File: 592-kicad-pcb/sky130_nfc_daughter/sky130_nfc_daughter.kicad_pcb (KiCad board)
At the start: 4 copper layers, 50 x 52 mm, 104 parts, among them J1 U.FL-R-SMT-1_80_, J10 U.FL-R-SMT-1_80_, J2 U.FL-R-SMT-1_80_, J3 U.FL-R-SMT-1_80_, J4 U.FL-R-SMT-1_80_, J5 U.FL-R-SMT-1_80_, J6 U.FL-R-SMT-1_80_, J7 U.FL-R-SMT-1_80_, J8 DF40C-40DS-0.4V_51_, J9 DF40C-40DS-0.4V_51_, SW1 SW_Push, U1 Caravel_QFN, U3 W25Q32JVZP

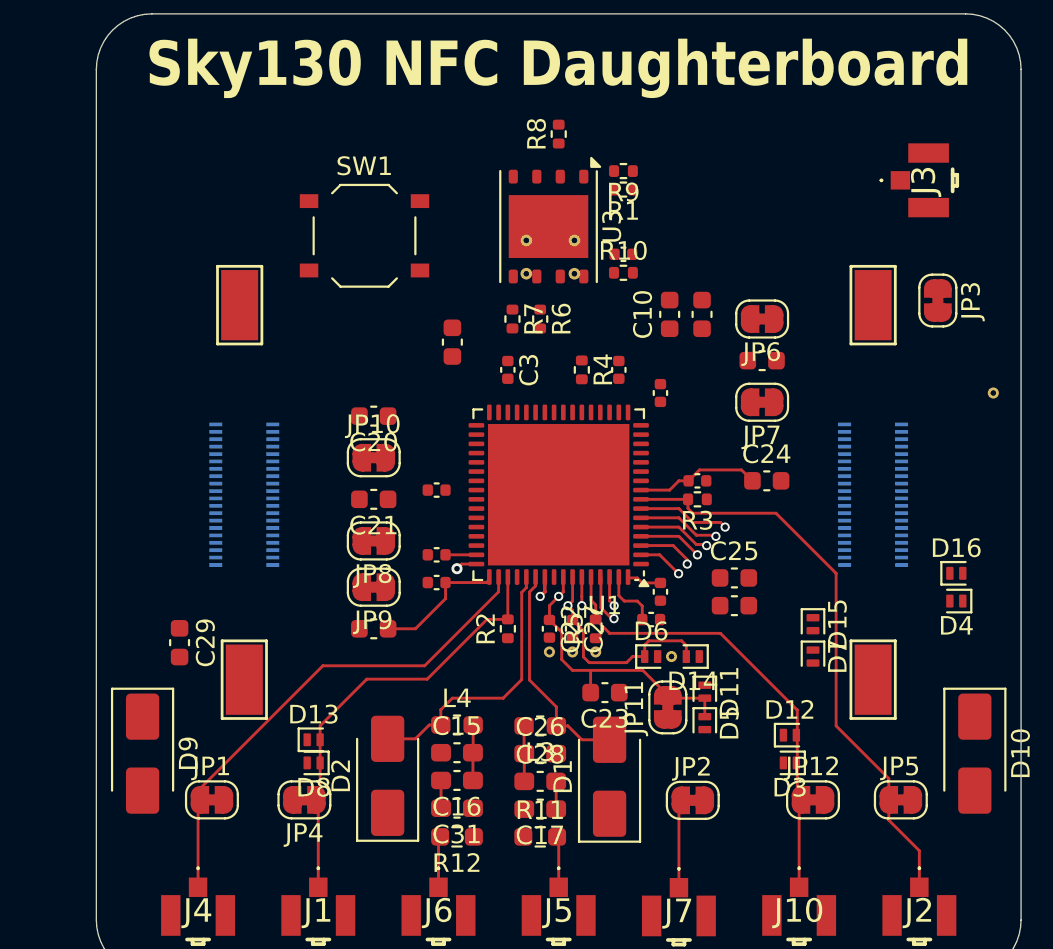
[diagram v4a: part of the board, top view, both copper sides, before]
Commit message: daughterboard routing, changed some mezzanine pins - more to come
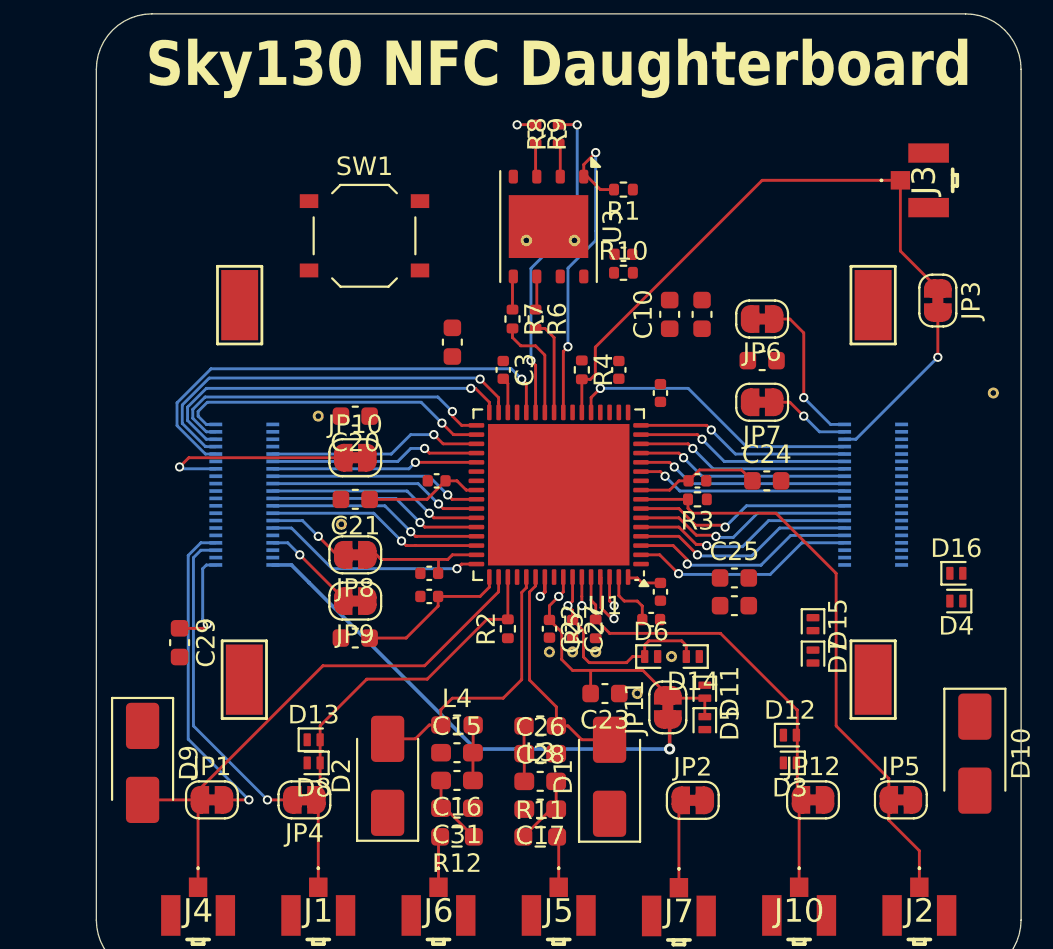
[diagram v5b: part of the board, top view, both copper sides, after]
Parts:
- removed the STITCHM1 at (75.3, 34.0)
- removed the STITCHM1 at (72.8, 34.0)
- added REF**: STITCHING_VIA_0p3mm, 592-partslib:STITCHING_VIA_0p3mm, F.Cu at (62.8, 47.6)
- added REF**: STITCHING_VIA_0p3mm, 592-partslib:STITCHING_VIA_0p3mm, F.Cu at (78.8, 56.8)
- added REF**: STITCHING_VIA_0p3mm, 592-partslib:STITCHING_VIA_0p3mm, F.Cu at (61.5, 41.8)
- moved R9 5.15 mm to (73.2, 26.5), turned to -90 degrees
- moved JP8 1.25 mm to (63.5, 49.2)
- moved JP9 1.25 mm to (63.5, 51.8)
- moved C18 1.12 mm to (63.5, 53.8)
- moved C11 1.08 mm to (67.5, 50.2)
- moved C20 1.00 mm to (63.5, 41.8)
- moved C21 1.00 mm to (63.5, 46.2)
- moved JP10 1.00 mm to (63.5, 44.0)
- moved C6 0.85 mm to (67.5, 51.5)
- moved C12 0.50 mm to (67.9, 45.2)
- moved D9 0.50 mm to (52.0, 60.5)
- moved C3 0.25 mm to (71.5, 39.2)
- moved R6 0.25 mm to (73.2, 36.5)
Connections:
- J8 pad 10: /jtag_TDO -> /gpio
- J8 pad 15: GND -> /spi_0_sck
- J8 pad 16: /spi_0_sck -> GND
- J8 pad 17: GND -> /reset_io
- J8 pad 18: /reset_io -> GND
- J8 pad 2: /gpio -> /jtag_TDO
- J8 pad 23: GND -> /i2c_0_sda
- J8 pad 24: /i2c_0_sda -> GND
- J8 pad 25: GND -> /i2c_0_scl
- J8 pad 26: /i2c_0_scl -> GND
- J8 pad 29: GND -> /tdo2
- J8 pad 3: /c_sel_inc -> GND
- J8 pad 30: /tdo2 -> GND
- J8 pad 4: /jtag_TCK -> /jtag_TDI
- J8 pad 8: /jtag_TDI -> /jtag_TCK
- J9 pad 10: GND -> /spi_flash_0_dq_3
- J9 pad 11: /spi_flash_0_dq_2 -> GND
- J9 pad 12: GND -> /spi_flash_0_dq_2
- J9 pad 13: /spi_flash_0_dq_1 -> GND
- J9 pad 14: GND -> /spi_flash_0_dq_1
- J9 pad 15: /spi_flash_0_dq_0 -> GND
- J9 pad 16: GND -> /spi_flash_0_dq_0
- J9 pad 17: /spi_flash_0_cs_0 -> GND
- J9 pad 18: GND -> /spi_flash_0_cs_0
- J9 pad 19: /spi_flash_0_sck -> GND
- J9 pad 20: /J_ext_clk_dig -> /spi_flash_0_sck
- J9 pad 22: /ext_reset_dig -> /J_ext_clk_dig
- J9 pad 24: GND -> /ext_reset_dig
- J9 pad 27: /TMS_EXT -> GND
- J9 pad 29: /TCK_EXT -> /RESET_EXT
- J9 pad 30: GND -> /TMS_EXT
- J9 pad 31: /TRST_EXT -> /J_FS_EXT
- J9 pad 32: /J_FS_EXT -> /TCK_EXT
- J9 pad 34: /RESET_EXT -> /TRST_EXT
- J9 pad 5: /J_clk -> GND
- J9 pad 6: GND -> /J_clk
- J9 pad 7: /reset_b -> GND
- J9 pad 8: GND -> /reset_b
- J9 pad 9: /spi_flash_0_dq_3 -> GND
- STITCHM1 pad 1: (no net) -> GND (x2)
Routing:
- net /clk: track 0.00 -> 31.0 mm
- net Net-(JP11-A): track 0.00 -> 27.2 mm, vias 0 -> 1
- net /gpio: track 0.00 -> 25.5 mm, vias 0 -> 1
- net /jtag_TCK: track 0.00 -> 22.3 mm, vias 0 -> 1
- net /jtag_TMS: track 0.00 -> 20.3 mm, vias 0 -> 1
- net /jtag_TDI: track 0.00 -> 18.4 mm, vias 0 -> 1
- net /flash_csb: track 0.00 -> 18.3 mm, vias 0 -> 2
- net /J_ANA_MUX_OUT_EXT: track 0.00 -> 17.7 mm, vias 0 -> 1
- net /flash_io1: track 0.00 -> 17.7 mm, vias 0 -> 2
- net /J_clock_uncore: track 0.00 -> 17.5 mm, vias 0 -> 1
- net /jtag_TDO: track 0.00 -> 17.4 mm, vias 0 -> 1
- net /reset_b: track 0.00 -> 16.0 mm, vias 0 -> 1
- net vdda_user_3v3: track 8.39 -> 20.2 mm
- net /i2c_0_scl: track 0.00 -> 11.7 mm, vias 0 -> 1
- net /i2c_0_sda: track 0.00 -> 11.7 mm, vias 0 -> 1
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
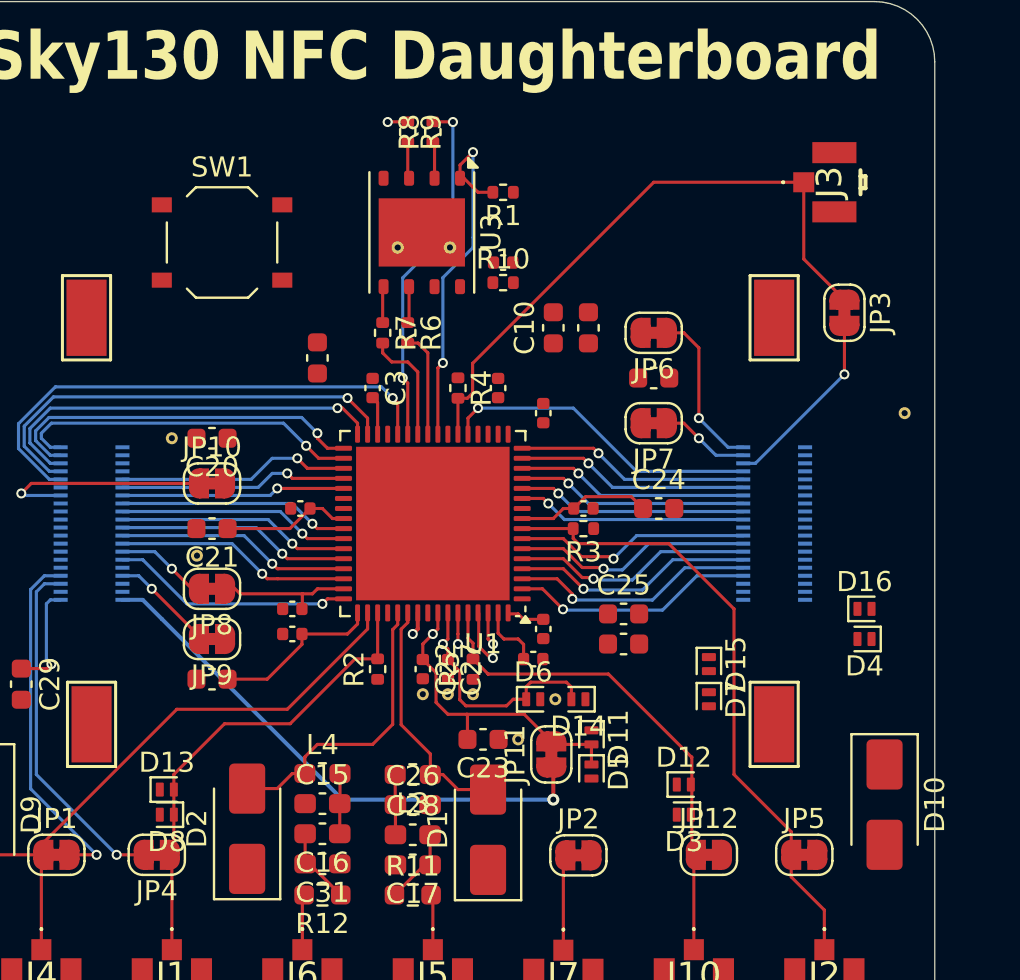
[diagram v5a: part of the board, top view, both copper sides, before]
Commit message: complete signal routing on daughterboard, TODO: power/gnd connections
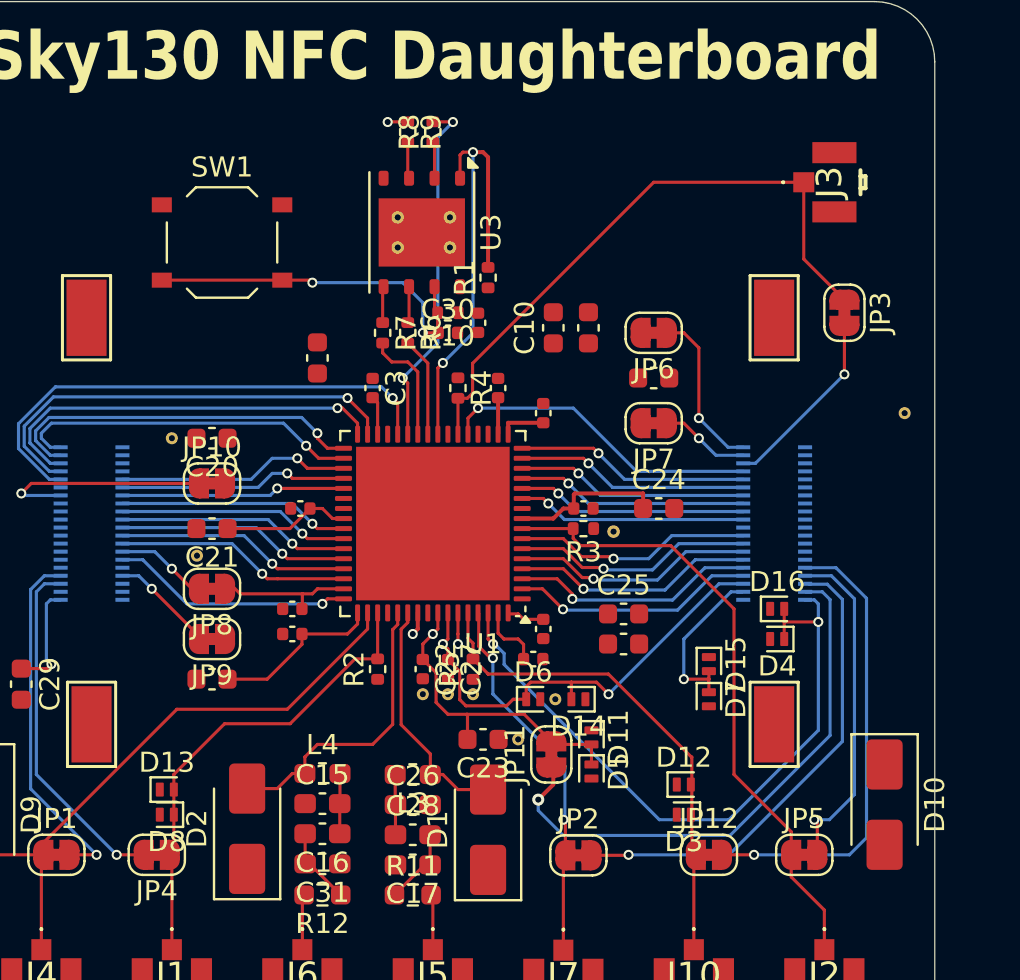
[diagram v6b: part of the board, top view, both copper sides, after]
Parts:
- added C30: 0.1uf, Capacitor_SMD:C_0402_1005Metric, F.Cu at (75.2, 36.5)
- added STITCHM1: StitchingVia-0.3mm, flyingcarsfootprints:StitchingVia-0.3mm, F.Cu at (72.8, 30.8)
- added STITCHM1: StitchingVia-0.3mm, flyingcarsfootprints:StitchingVia-0.3mm, F.Cu at (83.5, 46.4)
- added STITCHM1: StitchingVia-0.3mm, flyingcarsfootprints:StitchingVia-0.3mm, F.Cu at (75.3, 30.8)
- moved D16 4.35 mm to (91.7, 50.2)
- moved D4 4.35 mm to (91.7, 51.8)
- moved R1 4.32 mm to (77.2, 33.8), turned to 90 degrees
- moved C9 3.25 mm to (76.8, 36.0), turned to 90 degrees
- moved R10 3.13 mm to (75.2, 35.5), turned to 180 degrees
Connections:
- net Net-(JP10-A) renamed /JA_vdda_user_3v3
- net Net-(JP6-A) renamed /J_vccd_mgmt_1v8
- net Net-(JP7-A) renamed /J_vddio_vdda_mgmt_3v3
- net Net-(JP8-B) renamed /JB_vdda_user_3v3
- net Net-(JP9-B) renamed /J_vccd_user_1v8
- J8 pad 39: Net-(JP11-A) -> GND
- J9 pad 22: /J_ext_clk_dig -> GND
- J9 pad 29: /RESET_EXT -> GND
- J9 pad 33: /NFC_AFE_TDO_EXT -> /J_ext_clk_dig
- J9 pad 36: GND -> /VREF_EXT
- J9 pad 37: GND -> /J_VDD_EXT
- J9 pad 38: /VREF_EXT -> /RESET_EXT
- J9 pad 39: GND -> /NFC_AFE_TDO_EXT
- JP11 pad 1: Net-(JP11-A) -> /J_VDD_EXT
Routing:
- net /NFC_AFE_TDO_EXT: track 1.65 -> 33.9 mm, vias 1 -> 2
- net /J_VDD_EXT: track 0.00 -> 27.8 mm, vias 0 -> 1
- net Net-(JP11-A): track 27.2 -> 0.00 mm, vias 1 -> 0
- net /J_ANA_MUX_OUT_2_EXT: track 0.00 -> 24.1 mm, vias 0 -> 1
- net /J_FS_EXT: track 0.00 -> 23.2 mm, vias 0 -> 1
- net /flash_rstb: track 0.00 -> 18.1 mm, vias 0 -> 2
- net /J_ext_clk_dig: track 0.00 -> 17.0 mm, vias 0 -> 1
- net /VREF_EXT: track 12.0 -> 23.5 mm, vias 1 -> 2
- net /ANA_MUX_OUT_2_EXT: track 7.39 -> 18.8 mm, vias 1 -> 2
- net /RESET_EXT: track 1.55 -> 9.78 mm, vias 1 -> 2
- net /flash_csb: track 18.3 -> 23.0 mm
- net vddio_vdda_mgmt_3v3: track 4.81 -> 7.13 mm
- net vccd_mgmt_1v8: track 0.00 -> 1.82 mm
- net vdda_user_3v3: track 20.2 -> 21.2 mm

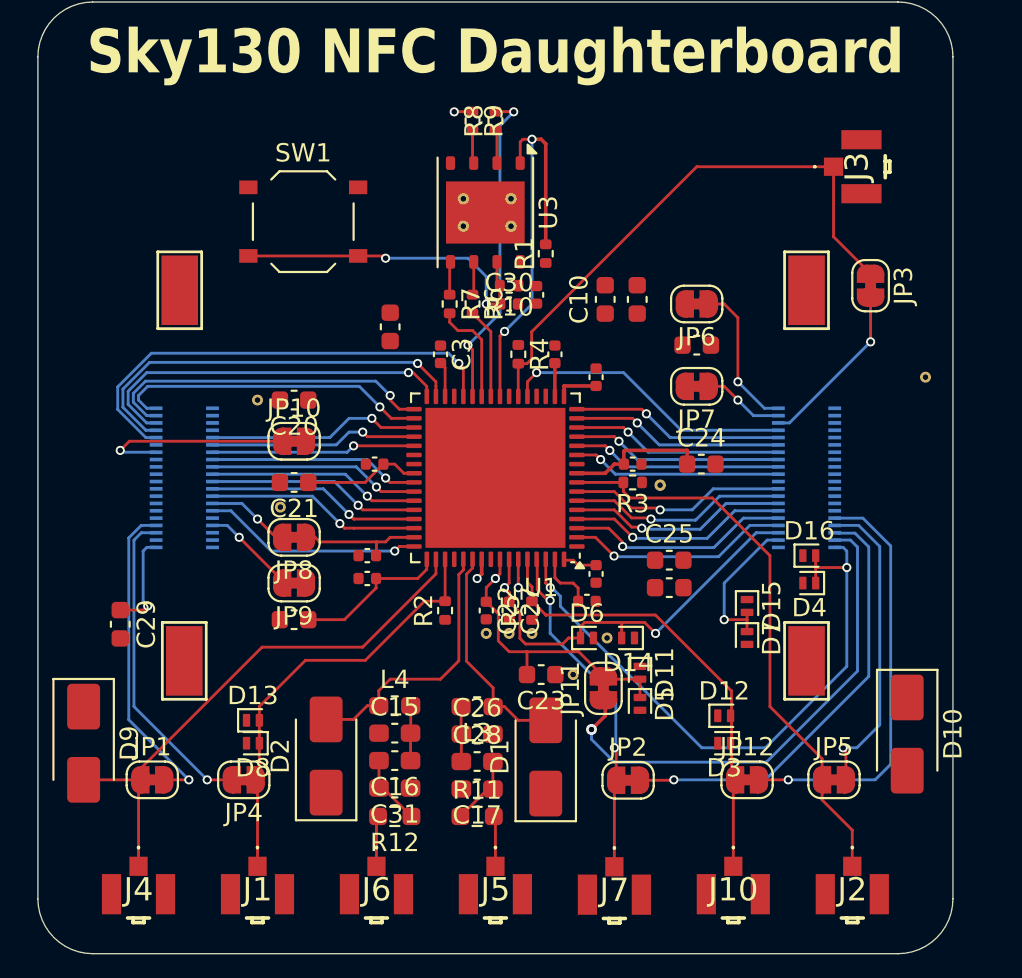
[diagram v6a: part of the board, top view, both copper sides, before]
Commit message: more daughterboard routing, power focus
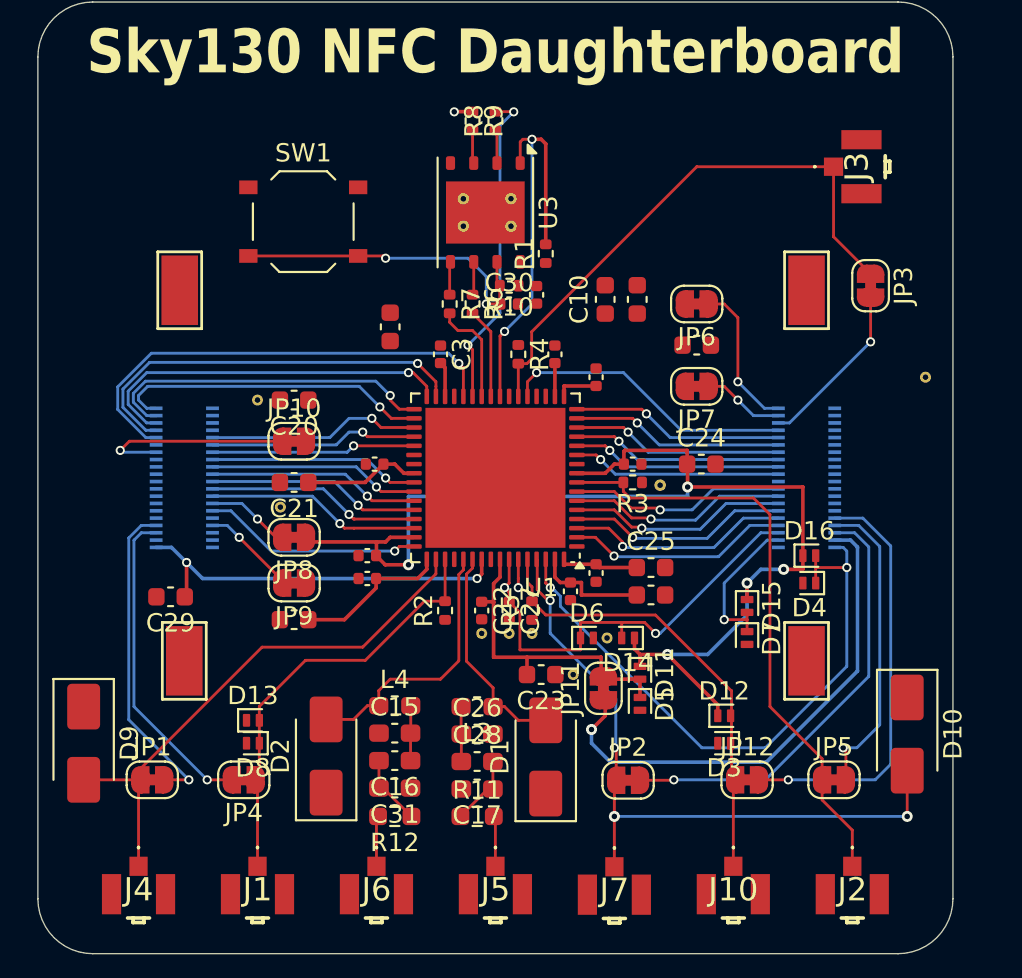
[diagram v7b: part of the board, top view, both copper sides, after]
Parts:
- moved C29 3.13 mm to (56.8, 52.5), turned to 180 degrees
- moved C14 1.08 mm to (83.0, 52.4)
- moved C25 1.08 mm to (83.0, 50.9)
- moved C5 1.05 mm to (78.6, 52.2), turned to 90 degrees
- moved C22 0.25 mm to (73.8, 53.2)
- moved REF** 0.25 mm to (73.8, 54.5)
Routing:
- net vdda_user_3v3: track 21.2 -> 74.0 mm, vias 0 -> 5
- net /ANA_MUX_OUT_2_EXT: track 18.8 -> 37.3 mm, vias 2 -> 4
- net /VRECT_OUT_EXT: track 6.64 -> 21.3 mm
- net vccd_user_1v8: track 11.7 -> 14.7 mm
- net vddio_vdda_mgmt_3v3: track 7.13 -> 9.89 mm
- net VDD_EXT: track 15.7 -> 17.0 mm, vias 1 -> 0
- net /ext_clk_dig: track 31.3 -> 32.7 mm
- net /VREF_EXT: track 23.5 -> 24.7 mm
